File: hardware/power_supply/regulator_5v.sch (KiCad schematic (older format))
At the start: 42 parts

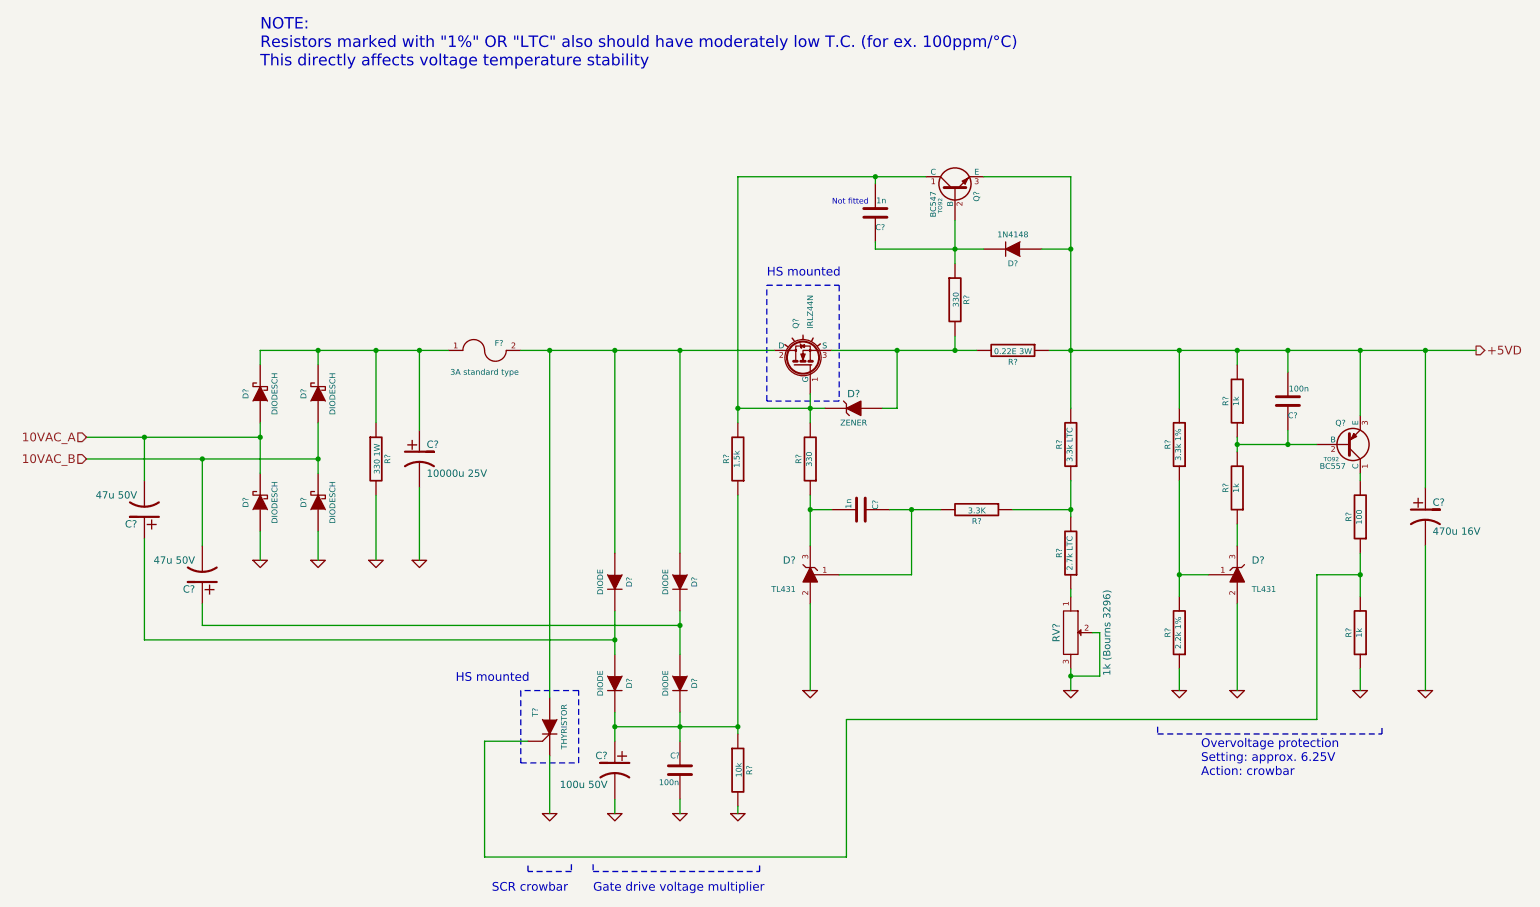
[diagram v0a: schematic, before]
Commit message: Update: added frequecy compensation nets in 5V regulator
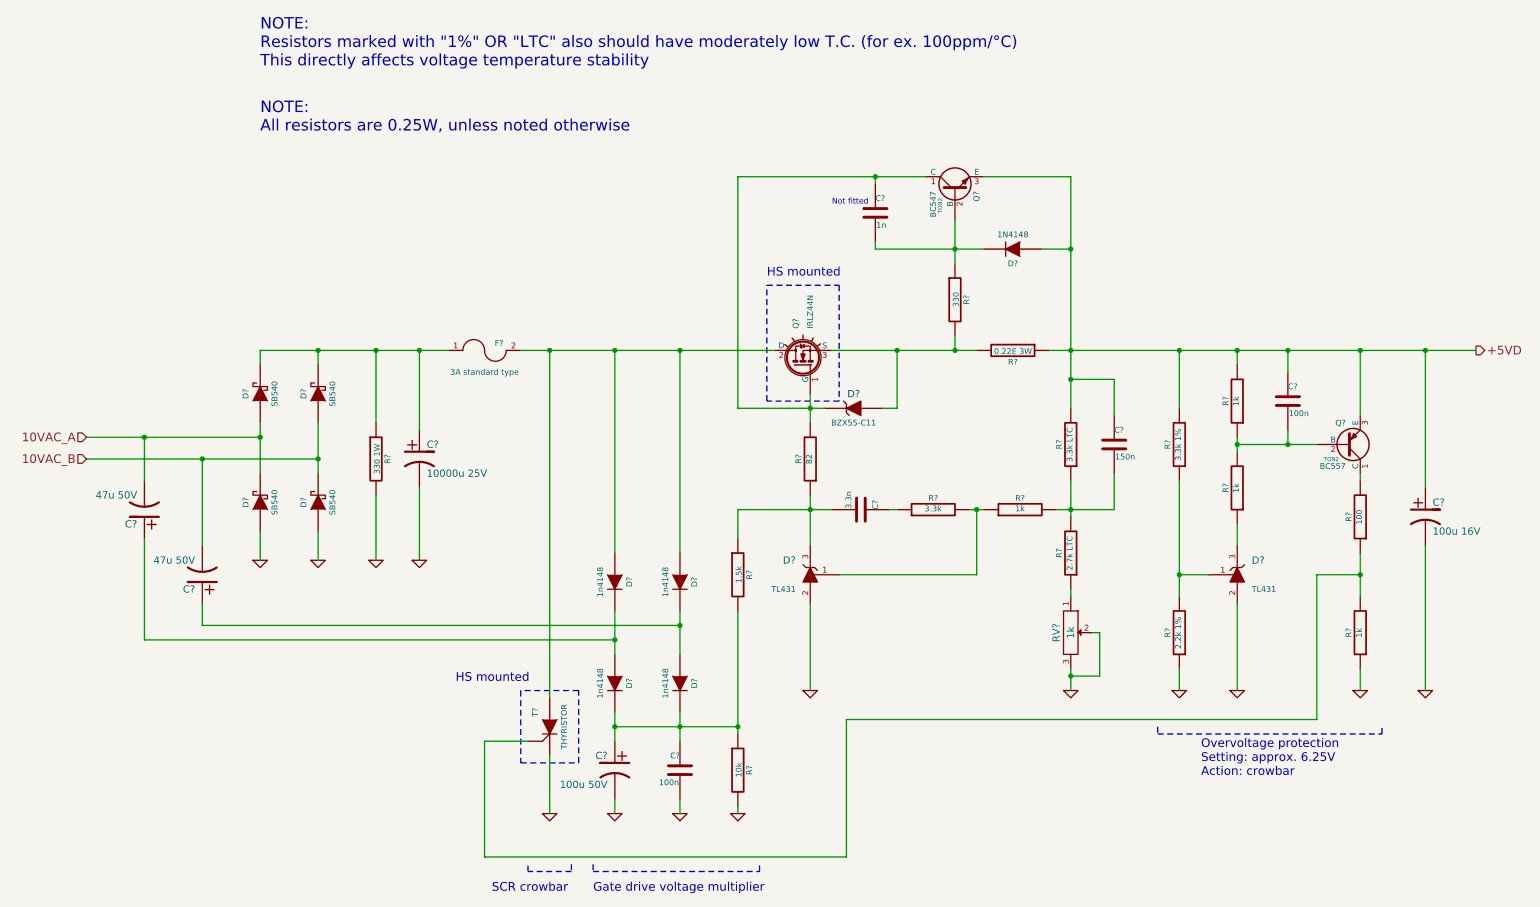
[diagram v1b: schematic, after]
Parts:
- added C?: 150n, symbol C
- added R?: 3.3k, symbol R
- C?: value 1n -> 3.3n
- C?: value 470u 16V -> 100u 16V
- D? (x4): value DIODESCH -> SB540
- D? (x4): value DIODE -> 1n4148
- D?: value ZENER -> BZX55-C11
- R?: value 330 -> 82
- R?: value 3.3K -> 1k
- RV?: value 1k (Bourns 3296) -> 1k; footprint (none) -> Bourns 3296W
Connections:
- net +5VD: now also C?.1, C?.1; no longer C?.2
- net at C?.1, C?.1, D?.2 (K)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: now also R?.2; no longer R?.1
- net at D?.2 (K), Q?.1 (C), Q?.1 (G)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: now also C?.1; no longer C?.2, R?.2
- net at D?.2 (K), Q?.2 (B), R?.1: now also C?.2; no longer C?.1
- net at C?.2, D?.3 (K), R?.1: now also R?.1
- net at R?.1, R?.2: now also R?.2, C?.2; no longer R?.1
- net at Q?.2 (B), R?.1, R?.2: now also C?.2; no longer C?.1
- new net: D?.1 (Ref), R?.1, R?.2
- new net: C?.1, R?.1
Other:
- note added: "NOTE:\nAll resistors are 0.25W, unless noted otherwise"
- moved on the sheet: R?
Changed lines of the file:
@@
 P 2300 3650
 F 0 "D?" H 2300 3750 40  0000 C CNN
-F 1 "DIODESCH" H 2300 3550 40  0000 C CNN
+F 1 "SB540" H 2300 3550 40  0000 C CNN
 F 2 "" H 2300 3650 60  0000 C CNN
 F 3 "" H 2300 3650 60  0000 C CNN
@@
 P 2700 3650
 F 0 "D?" H 2700 3750 40  0000 C CNN
-F 1 "DIODESCH" H 2700 3550 40  0000 C CNN
+F 1 "SB540" H 2700 3550 40  0000 C CNN
 F 2 "" H 2700 3650 60  0000 C CNN
 F 3 "" H 2700 3650 60  0000 C CNN
@@
 P 2300 4400
 F 0 "D?" H 2300 4500 40  0000 C CNN
-F 1 "DIODESCH" H 2300 4300 40  0000 C CNN
+F 1 "SB540" H 2300 4300 40  0000 C CNN
 F 2 "" H 2300 4400 60  0000 C CNN
 F 3 "" H 2300 4400 60  0000 C CNN
@@
 P 2700 4400
 F 0 "D?" H 2700 4500 40  0000 C CNN
-F 1 "DIODESCH" H 2700 4300 40  0000 C CNN
+F 1 "SB540" H 2700 4300 40  0000 C CNN
 F 2 "" H 2700 4400 60  0000 C CNN
 F 3 "" H 2700 4400 60  0000 C CNN
@@
 P 4750 4950
 F 0 "D?" H 4750 5050 40  0000 C CNN
-F 1 "DIODE" H 4750 4850 40  0000 C CNN
+F 1 "1n4148" H 4750 4850 40  0000 C CNN
 F 2 "" H 4750 4950 60  0000 C CNN
 F 3 "" H 4750 4950 60  0000 C CNN
@@
 P 5200 5650
 F 0 "D?" H 5200 5750 40  0000 C CNN
-F 1 "DIODE" H 5200 5550 40  0000 C CNN
+F 1 "1n4148" H 5200 5550 40  0000 C CNN
 F 2 "" H 5200 5650 60  0000 C CNN
 F 3 "" H 5200 5650 60  0000 C CNN
@@
 P 4750 5650
 F 0 "D?" H 4750 5750 40  0000 C CNN
-F 1 "DIODE" H 4750 5550 40  0000 C CNN
+F 1 "1n4148" H 4750 5550 40  0000 C CNN
 F 2 "" H 4750 5650 60  0000 C CNN
 F 3 "" H 4750 5650 60  0000 C CNN
@@
 P 5200 4950
 F 0 "D?" H 5200 5050 40  0000 C CNN
-F 1 "DIODE" H 5200 4850 40  0000 C CNN
+F 1 "1n4148" H 5200 4850 40  0000 C CNN
 F 2 "" H 5200 4950 60  0000 C CNN
 F 3 "" H 5200 4950 60  0000 C CNN
@@
 L R R?
 U 1 1 5317C2F5
-P 5600 4100
-F 0 "R?" V 5680 4100 40  0000 C CNN
-F 1 "1.5k" V 5607 4101 40  0000 C CNN
-F 2 "" V 5530 4100 30  0000 C CNN
-F 3 "" H 5600 4100 30  0000 C CNN
-	1    5600 4100
-	-1   0    0    1
+P 5600 4900
+F 0 "R?" V 5680 4900 40  0000 C CNN
+F 1 "1.5k" V 5607 4901 40  0000 C CNN
+F 2 "" V 5530 4900 30  0000 C CNN
+F 3 "" H 5600 4900 30  0000 C CNN
+	1    5600 4900
+	1    0    0    -1
 $EndComp
 $Comp
@@
 F 3 "" H 6550 2400 60  0000 C CNN
 	1    6550 2400
-	1    0    0    1
+	1    0    0    -1
 $EndComp
 $Comp
@@
 P 6400 3750
 F 0 "D?" H 6400 3850 50  0000 C CNN
-F 1 "ZENER" H 6400 3650 40  0000 C CNN
+F 1 "BZX55-C11" H 6400 3650 40  0000 C CNN
 F 2 "" H 6400 3750 60  0000 C CNN
 F 3 "" H 6400 3750 60  0000 C CNN
@@
 P 6100 4100
 F 0 "R?" V 6180 4100 40  0000 C CNN
-F 1 "330" V 6107 4101 40  0000 C CNN
+F 1 "82" V 6107 4101 40  0000 C CNN
 F 2 "" V 6030 4100 30  0000 C CNN
 F 3 "" H 6100 4100 30  0000 C CNN
@@
 P 6450 4450
 F 0 "C?" H 6450 4550 40  0000 L CNN
-F 1 "1n" H 6456 4365 40  0000 L CNN
+F 1 "3.3n" H 6456 4365 40  0000 L CNN
 F 2 "" H 6488 4300 30  0000 C CNN
 F 3 "" H 6450 4450 60  0000 C CNN
@@
 L R R?
 U 1 1 5317D418
-P 7250 4450
-F 0 "R?" V 7330 4450 40  0000 C CNN
-F 1 "3.3K" V 7257 4451 40  0000 C CNN
-F 2 "" V 7180 4450 30  0000 C CNN
-F 3 "" H 7250 4450 30  0000 C CNN
-	1    7250 4450
-	0    1    1    0
+P 7550 4450
+F 0 "R?" V 7630 4450 40  0000 C CNN
+F 1 "1k" V 7557 4451 40  0000 C CNN
+F 2 "" V 7480 4450 30  0000 C CNN
+F 3 "" H 7550 4450 30  0000 C CNN
+	1    7550 4450
+	0    -1   -1   0
 $EndComp
 $Comp
@@
 P 7900 5300
 F 0 "RV?" H 7900 5200 50  0000 C CNN
-F 1 "1k (Bourns 3296)" H 7900 5550 50  0000 C CNN
-F 2 "" H 7900 5300 60  0000 C CNN
+F 1 "1k" H 7900 5300 50  0000 C CNN
+F 2 "Bourns 3296W" H 7900 5300 60  0001 C CNN
 F 3 "" H 7900 5300 60  0000 C CNN
 	1    7900 5300
@@
 P 10350 4500
 F 0 "C?" H 10400 4600 50  0000 L CNN
-F 1 "470u 16V" H 10400 4400 50  0000 L CNN
+F 1 "100u 16V" H 10400 4400 50  0000 L CNN
 F 2 "" H 10350 4500 60  0000 C CNN
 F 3 "" H 10350 4500 60  0000 C CNN
@@
 $EndComp
 Wire Wire Line
-	1100 3950 1500 3950
-Wire Wire Line
-	1500 3950 2300 3950
-Wire Wire Line
-	2300 3850 2300 3950
-Wire Wire Line
-	2300 3950 2300 4200
-Wire Wire Line
-	1100 4100 1900 4100
-Wire Wire Line
-	1900 4100 2700 4100
-Wire Wire Line
-	2700 3850 2700 4100
-Wire Wire Line
-	2700 4100 2700 4200
+	1100 3950 2300 3950
+Wire Wire Line
+	2300 3850 2300 4200
+Wire Wire Line
+	1100 4100 2700 4100
+Wire Wire Line
+	2700 3850 2700 4200
 Connection ~ 2700 4100
 Connection ~ 2300 3950
 Wire Wire Line
-	2300 3350 2700 3350
-Wire Wire Line
-	2700 3350 3100 3350
-Wire Wire Line
-	3100 3350 3400 3350
-Wire Wire Line
-	3400 3350 3600 3350
-Wire Wire Line
-	4100 3350 4300 3350
-Wire Wire Line
-	4300 3350 4750 3350
-Wire Wire Line
-	4750 3350 5200 3350
-Wire Wire Line
-	5200 3350 5850 3350
+	2300 3350 3600 3350
+Wire Wire Line
+	4100 3350 5850 3350
 Wire Wire Line
 	2700 3350 2700 3450
@@
 	5200 6450 5200 6550
 Wire Wire Line
-	5200 5850 5200 5950
-Wire Wire Line
-	5200 5950 5200 6050
-Wire Wire Line
-	5600 4350 5600 5950
-Wire Wire Line
-	5600 5950 5600 6000
+	5200 5850 5200 6050
+Wire Wire Line
+	5600 5150 5600 6000
 Connection ~ 5200 5950
 Wire Wire Line
@@
 Connection ~ 3100 3350
 Wire Wire Line
-	6250 3350 6700 3350
-Wire Wire Line
-	6700 3350 7100 3350
-Wire Wire Line
-	7100 3350 7250 3350
+	6250 3350 7250 3350
 Connection ~ 5600 5950
 Connection ~ 6700 3350
 Wire Wire Line
-	7750 3350 7900 3350
-Wire Wire Line
-	7900 3350 8650 3350
-Wire Wire Line
-	8650 3350 9050 3350
-Wire Wire Line
-	9050 3350 9400 3350
-Wire Wire Line
-	9400 3350 9900 3350
-Wire Wire Line
-	9900 3350 10350 3350
-Wire Wire Line
-	10350 3350 10700 3350
+	7750 3350 10700 3350
 Wire Wire Line
 	6100 5100 6100 5700
@@
 	8100 5600 7900 5600
 Wire Wire Line
-	7900 5550 7900 5600
-Wire Wire Line
-	7900 5600 7900 5700
+	7900 5550 7900 5700
 Connection ~ 7900 5600
 Wire Wire Line
 	6700 3350 6700 3750
 Wire Wire Line
-	7100 2450 7100 2650
-Wire Wire Line
-	7100 2650 7100 2750
+	7100 2450 7100 2750
 Connection ~ 7100 2650
 Wire Wire Line
@@
 Connection ~ 7900 2650
 Wire Wire Line
-	7900 2150 7900 2650
-Wire Wire Line
-	7900 2650 7900 3350
-Wire Wire Line
-	7900 3350 7900 3750
-Wire Wire Line
-	5600 2150 6550 2150
-Wire Wire Line
-	6550 2150 6900 2150
-Wire Wire Line
-	5600 3750 6100 3750
-Wire Wire Line
-	6100 3750 6200 3750
+	7900 2150 7900 3750
+Wire Wire Line
+	5600 2150 6900 2150
+Wire Wire Line
+	5600 3750 6200 3750
 Wire Wire Line
 	10350 4700 10350 5700
@@
 Connection ~ 7100 3350
 Wire Wire Line
-	6550 2650 7100 2650
-Wire Wire Line
-	7100 2650 7300 2650
-Wire Wire Line
-	6100 3650 6100 3750
-Wire Wire Line
-	6100 3750 6100 3850
-Wire Wire Line
-	6100 4350 6100 4450
-Wire Wire Line
-	6100 4450 6100 4700
-Wire Wire Line
-	6250 4450 6100 4450
+	6550 2650 7300 2650
+Wire Wire Line
+	6100 3650 6100 3850
+Wire Wire Line
+	6100 4350 6100 4700
+Wire Wire Line
+	5600 4450 6250 4450
 Connection ~ 6100 4450
 Wire Wire Line
-	6650 4450 6800 4450
-Wire Wire Line
-	6800 4450 7000 4450
-Wire Wire Line
-	6800 4450 6800 4900
-Wire Wire Line
-	6800 4900 6300 4900
-Connection ~ 6800 4450
-Wire Wire Line
-	5600 2150 5600 3750
-Wire Wire Line
-	5600 3750 5600 3850
+	6300 4900 7250 4900
 Wire Wire Line
 	6550 2150 6550 2200
@@
 F 3 "" H 9400 3700 60  0000 C CNN
 	1    9400 3700
-	1    0    0    1
+	1    0    0    -1
 $EndComp
 $Comp
@@
 Connection ~ 8650 3350
 Wire Wire Line
-	9050 4000 9400 4000
-Wire Wire Line
-	9400 4000 9600 4000
-Wire Wire Line
-	9050 3950 9050 4000
-Wire Wire Line
-	9050 4000 9050 4050
+	9050 4000 9600 4000
+Wire Wire Line
+	9050 3950 9050 4050
 Connection ~ 9050 4000
 Wire Wire Line
@@
 Connection ~ 9400 4000
 Wire Wire Line
-	8650 4250 8650 4900
-Wire Wire Line
-	8650 4900 8650 5050
+	8650 4250 8650 5050
 Wire Wire Line
 	8650 4900 8850 4900
@@
 	9900 5550 9900 5700
 Wire Wire Line
-	9900 4750 9900 4900
-Wire Wire Line
-	9900 4900 9900 5050
+	9900 4750 9900 5050
 Wire Wire Line
 	9900 4200 9900 4250
 Wire Wire Line
-	7900 4250 7900 4450
-Wire Wire Line
-	7900 4450 7900 4500
-Wire Wire Line
-	7500 4450 7900 4450
+	7900 4250 7900 4500
 Connection ~ 7900 4450
 Wire Wire Line
@@
 Wire Wire Line
 	1900 4100 1900 4700
-Connection ~ 5600 3750
-Wire Wire Line
-	4750 5850 4750 5950
-Wire Wire Line
-	4750 5950 4750 6050
-Wire Wire Line
-	4750 5950 5200 5950
-Wire Wire Line
-	5200 5950 5600 5950
+Wire Wire Line
+	4750 5850 4750 6050
+Wire Wire Line
+	4750 5950 5600 5950
 Wire Wire Line
 	1900 5100 1900 5250
@@
 	1900 5250 5200 5250
 Wire Wire Line
-	5200 5150 5200 5250
-Wire Wire Line
-	5200 5250 5200 5450
+	5200 5150 5200 5450
 Wire Wire Line
 	1500 4650 1500 5350
@@
 	1500 5350 4750 5350
 Wire Wire Line
-	4750 5150 4750 5350
-Wire Wire Line
-	4750 5350 4750 5450
+	4750 5150 4750 5450
 Connection ~ 4750 5350
 Connection ~ 5200 5250
@@
 Text Notes 6250 2350 0    39   ~ 0
 Not fitted
+$Comp
+L R R?
+U 1 1 5320E3A0
+P 6950 4450
+F 0 "R?" V 7030 4450 40  0000 C CNN
+F 1 "3.3k" V 6957 4451 40  0000 C CNN
+F 2 "" V 6880 4450 30  0000 C CNN
+F 3 "" H 6950 4450 30  0000 C CNN
+	1    6950 4450
+	0    -1   -1   0
+$EndComp
+Wire Wire Line
+	6650 4450 6700 4450
+Wire Wire Line
+	7800 4450 8200 4450
+Wire Wire Line
+	7200 4450 7300 4450
+Wire Wire Line
+	7250 4900 7250 4450
+Connection ~ 7250 4450
+$Comp
+L C C?
+U 1 1 5320E64E
+P 8200 4000
+F 0 "C?" H 8200 4100 40  0000 L CNN
+F 1 "150n" H 8206 3915 40  0000 L CNN
+F 2 "" H 8238 3850 30  0000 C CNN
+F 3 "" H 8200 4000 60  0000 C CNN
+	1    8200 4000
+	1    0    0    -1
+$EndComp
+Wire Wire Line
+	8200 3800 8200 3550
+Wire Wire Line
+	8200 3550 7900 3550
+Connection ~ 7900 3550
+Wire Wire Line
+	8200 4450 8200 4200
+Wire Wire Line
+	5600 4650 5600 4450
+Wire Wire Line
+	5600 2150 5600 3750
+Text Notes 2300 1850 0    79   ~ 0
+NOTE:\nAll resistors are 0.25W, unless noted otherwise
 $EndSCHEMATC

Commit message: Update: +-15V regulator schematic almost complete
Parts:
- removed RV?: 1k, Bourns 3296W, symbol POT
- added C?: 100n, symbol C
- added VR?: 1k 3296W, symbol R_POT
- C? (x2): value 47u 50V -> 47u 35V
- D? (x4): value 1n4148 -> 1N4148
- R?: value 3.3k LTC -> 2.7k LTC
- R?: value 2.7k LTC -> 2.2k LTC
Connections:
- net GND: now also C?.2, VR?.2, VR?.3
- net at C?.1, D?.2 (K), D?.2 (K)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: now also C?.1
- net at R?.1: now also VR?.1
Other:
- note removed: "NOTE:\nAll resistors are 0.25W, unless noted otherwise"
- note removed: "NOTE:\nResistors marked with "1%" OR "LTC" also should have moderately low T.C. (for ex. 100ppm/°C)\nThis directly affects voltage temperature stability"
- moved on the sheet: C?
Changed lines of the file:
@@
 LIBS:irlz44n
 LIBS:tl431
+LIBS:r_pot
 LIBS:power_supply-cache
 EELAYER 24 0
@@
 $Descr A4 11693 8268
 encoding utf-8
-Sheet 2 2
+Sheet 2 3
 Title "+5V 2.0A voltage regulator"
 Date "06 марта 2014"
@@
 P 1500 4450
 F 0 "C?" H 1550 4550 50  0000 L CNN
-F 1 "47u 50V" H 1550 4350 50  0000 L CNN
+F 1 "47u 35V" H 1550 4350 50  0000 L CNN
 F 2 "" H 1500 4450 60  0000 C CNN
 F 3 "" H 1500 4450 60  0000 C CNN
@@
 P 1900 4900
 F 0 "C?" H 1950 5000 50  0000 L CNN
-F 1 "47u 50V" H 1950 4800 50  0000 L CNN
+F 1 "47u 35V" H 1950 4800 50  0000 L CNN
 F 2 "" H 1900 4900 60  0000 C CNN
 F 3 "" H 1900 4900 60  0000 C CNN
@@
 P 4750 4950
 F 0 "D?" H 4750 5050 40  0000 C CNN
-F 1 "1n4148" H 4750 4850 40  0000 C CNN
+F 1 "1N4148" H 4750 4850 40  0000 C CNN
 F 2 "" H 4750 4950 60  0000 C CNN
 F 3 "" H 4750 4950 60  0000 C CNN
@@
 P 5200 5650
 F 0 "D?" H 5200 5750 40  0000 C CNN
-F 1 "1n4148" H 5200 5550 40  0000 C CNN
+F 1 "1N4148" H 5200 5550 40  0000 C CNN
 F 2 "" H 5200 5650 60  0000 C CNN
 F 3 "" H 5200 5650 60  0000 C CNN
@@
 P 4750 5650
 F 0 "D?" H 4750 5750 40  0000 C CNN
-F 1 "1n4148" H 4750 5550 40  0000 C CNN
+F 1 "1N4148" H 4750 5550 40  0000 C CNN
 F 2 "" H 4750 5650 60  0000 C CNN
 F 3 "" H 4750 5650 60  0000 C CNN
@@
 P 5200 4950
 F 0 "D?" H 5200 5050 40  0000 C CNN
-F 1 "1n4148" H 5200 4850 40  0000 C CNN
+F 1 "1N4148" H 5200 4850 40  0000 C CNN
 F 2 "" H 5200 4950 60  0000 C CNN
 F 3 "" H 5200 4950 60  0000 C CNN
@@
 L CP1 C?
 U 1 1 5317BBD7
-P 3400 4100
-F 0 "C?" H 3450 4200 50  0000 L CNN
-F 1 "10000u 25V" H 3450 4000 50  0000 L CNN
-F 2 "" H 3400 4100 60  0000 C CNN
-F 3 "" H 3400 4100 60  0000 C CNN
-	1    3400 4100
+P 3750 4100
+F 0 "C?" H 3800 4200 50  0000 L CNN
+F 1 "10000u 25V" H 3800 4000 50  0000 L CNN
+F 2 "" H 3750 4100 60  0000 C CNN
+F 3 "" H 3750 4100 60  0000 C CNN
+	1    3750 4100
 	1    0    0    -1
 $EndComp
@@
 P 7900 4000
 F 0 "R?" V 7980 4000 40  0000 C CNN
-F 1 "3.3k LTC" V 7907 4001 40  0000 C CNN
+F 1 "2.7k LTC" V 7907 4001 40  0000 C CNN
 F 2 "" V 7830 4000 30  0000 C CNN
 F 3 "" H 7900 4000 30  0000 C CNN
@@
 P 7900 4750
 F 0 "R?" V 7980 4750 40  0000 C CNN
-F 1 "2.7k LTC" V 7907 4751 40  0000 C CNN
+F 1 "2.2k LTC" V 7907 4751 40  0000 C CNN
 F 2 "" V 7830 4750 30  0000 C CNN
 F 3 "" H 7900 4750 30  0000 C CNN
 	1    7900 4750
 	-1   0    0    1
-$EndComp
-$Comp
-L POT RV?
-U 1 1 5317D8F0
-P 7900 5300
-F 0 "RV?" H 7900 5200 50  0000 C CNN
-F 1 "1k" H 7900 5300 50  0000 C CNN
-F 2 "Bourns 3296W" H 7900 5300 60  0001 C CNN
-F 3 "" H 7900 5300 60  0000 C CNN
-	1    7900 5300
-	0    1    1    0
 $EndComp
 $Comp
@@
 Text Notes 3900 7100 0    60   ~ 0
 SCR crowbar
-Text Notes 2300 1400 0    79   ~ 0
-NOTE:\nResistors marked with "1%" OR "LTC" also should have moderately low T.C. (for ex. 100ppm/°C)\nThis directly affects voltage temperature stability
 Wire Notes Line
 	4100 5700 4100 6200
@@
 Wire Wire Line
 	5600 2150 5600 3750
-Text Notes 2300 1850 0    79   ~ 0
-NOTE:\nAll resistors are 0.25W, unless noted otherwise
+$Comp
+L C C?
+U 1 1 5323196D
+P 3400 4100
+F 0 "C?" H 3400 4200 40  0000 L CNN
+F 1 "100n" H 3406 4015 40  0000 L CNN
+F 2 "" H 3438 3950 30  0000 C CNN
+F 3 "" H 3400 4100 60  0000 C CNN
+	1    3400 4100
+	1    0    0    -1
+$EndComp
+Wire Wire Line
+	3750 3900 3750 3750
+Wire Wire Line
+	3750 3750 3400 3750
+Connection ~ 3400 3750
+Wire Wire Line
+	3750 4300 3750 4450
+Wire Wire Line
+	3750 4450 3400 4450
+Connection ~ 3400 4450
+$Comp
+L R_POT VR?
+U 1 1 53239788
+P 7900 5300
+F 0 "VR?" V 7900 5300 40  0000 C CNN
+F 1 "1k 3296W" V 7800 5300 40  0000 C CNN
+F 2 "" V 7830 5300 30  0000 C CNN
+F 3 "" H 7900 5300 30  0000 C CNN
+	1    7900 5300
+	1    0    0    -1
+$EndComp
 $EndSCHEMATC
